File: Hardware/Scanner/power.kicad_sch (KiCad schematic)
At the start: 15 parts, among them J1 I2C ThroughHole, J3 I2C, J4 Interface, U7 AP7312-1833W6-7

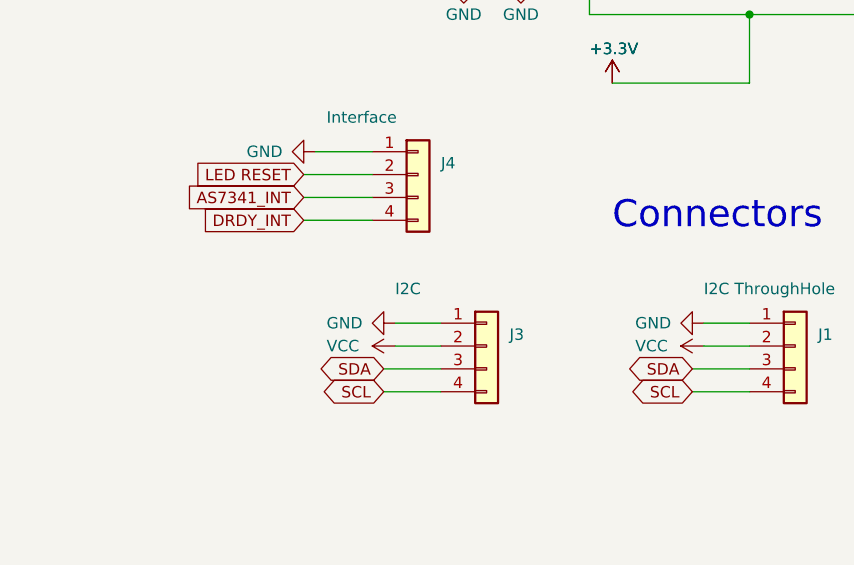
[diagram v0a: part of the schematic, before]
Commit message: added footprint for MTSM2601SMF1-100
Signed-off-by: lokimetasmith <lokimail@gmail.com>
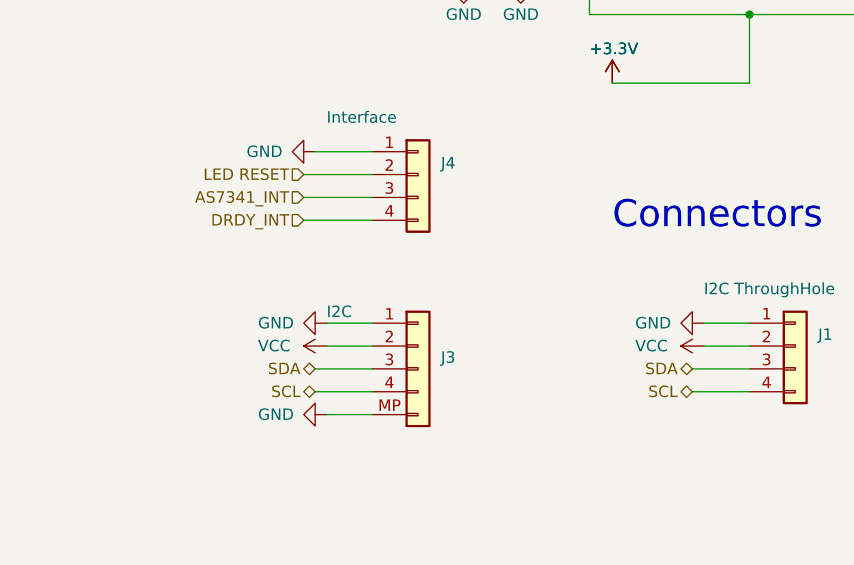
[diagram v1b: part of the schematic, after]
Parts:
- J3: symbol Connector_Generic:Conn_01x04 -> Connector_Generic:Conn_01x05
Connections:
- net GND: now also J3.MP (Pin_5)

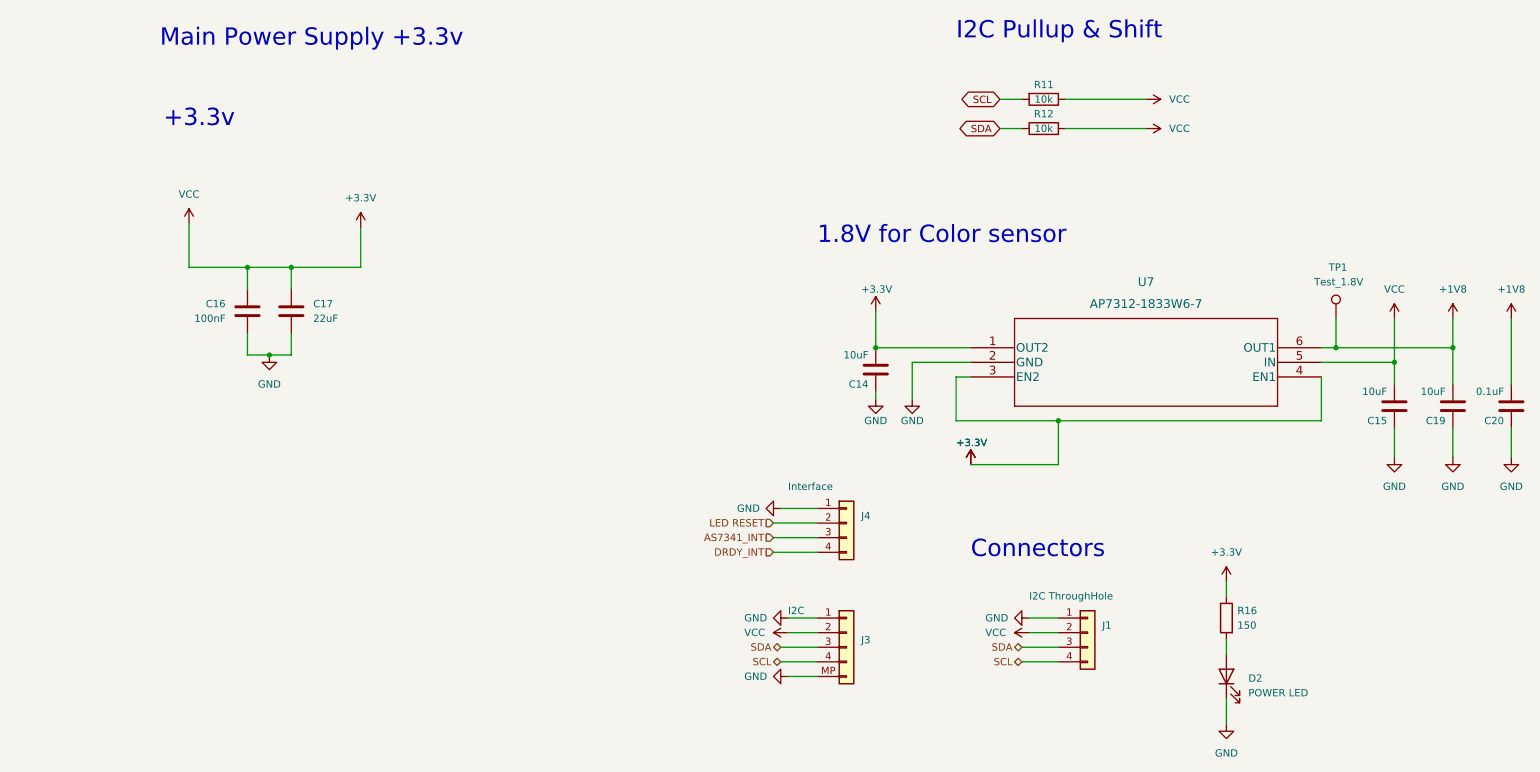
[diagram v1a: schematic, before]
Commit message: lots of changes, added footprints, fixed broken schemaitcs, fixed kicad 7.0 issues
Signed-off-by: lokimetasmith <lokimail@gmail.com>
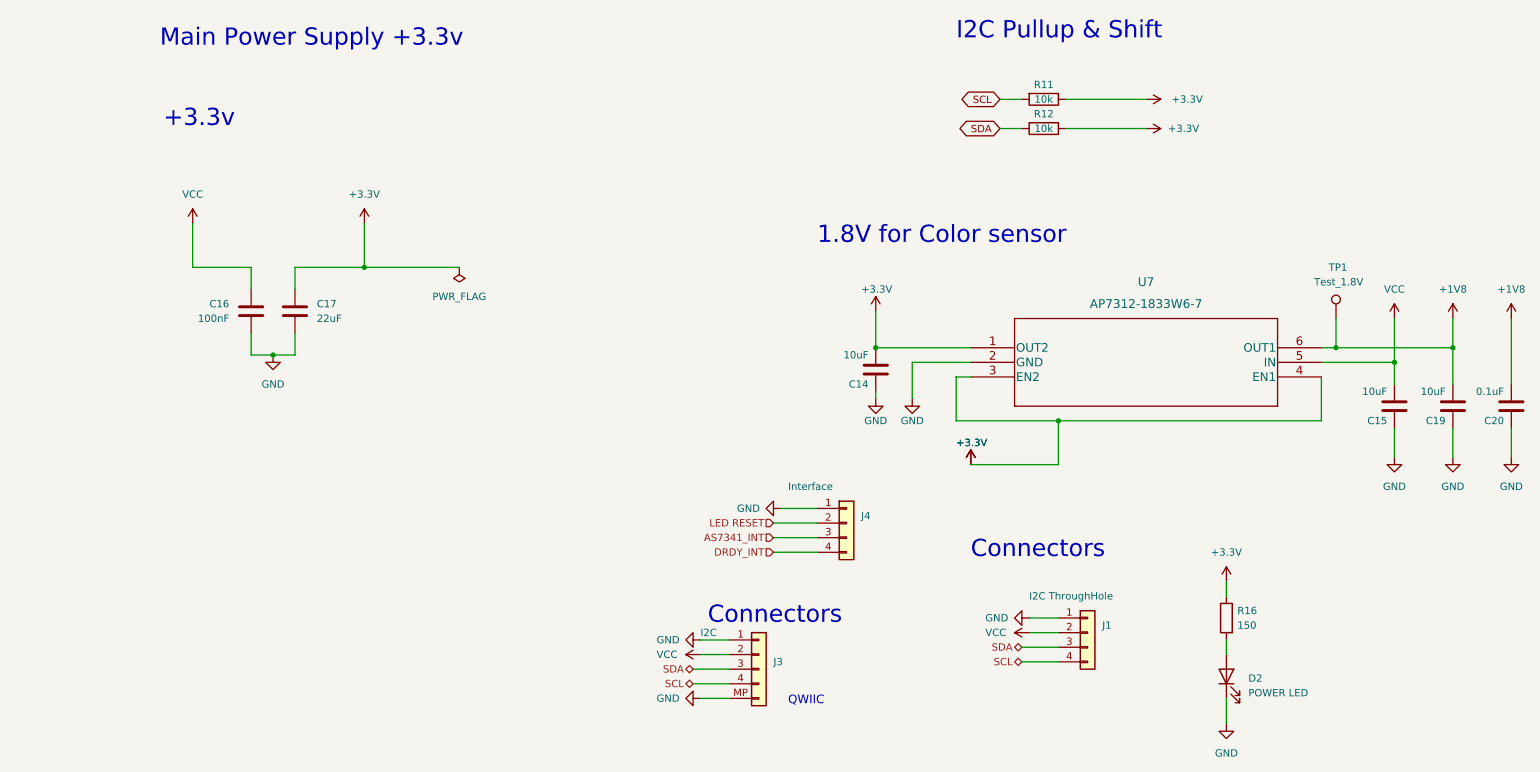
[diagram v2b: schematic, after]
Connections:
- net +3V3 renamed +3.3V
- net +3.3V: no longer C15.2, C16.2, J1.2 (Pin_2), J3.2 (Pin_2), U7.5 (IN)
- new net VCC: C15.2, C16.2, J1.2 (Pin_2), J3.2 (Pin_2), U7.5 (IN)
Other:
- note added: "QWIIC"
- moved on the sheet: C16, C17, J3

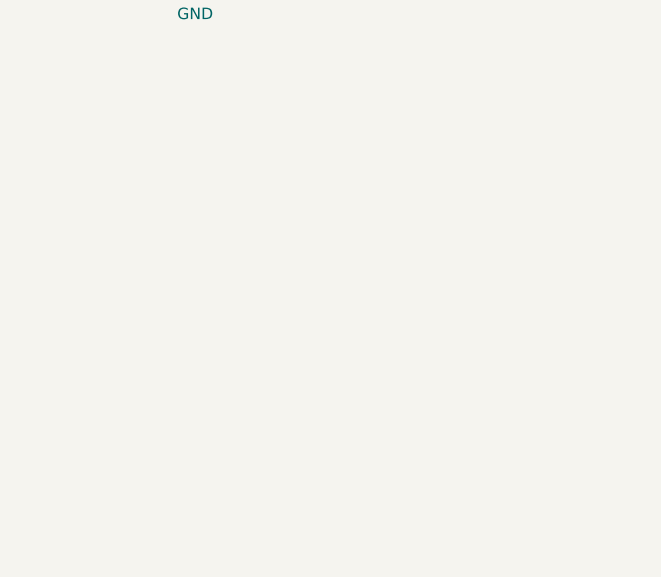
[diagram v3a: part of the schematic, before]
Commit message: added options for using internal adc, external adc, or 3.3v
Signed-off-by: lokimetasmith <lokimail@gmail.com>
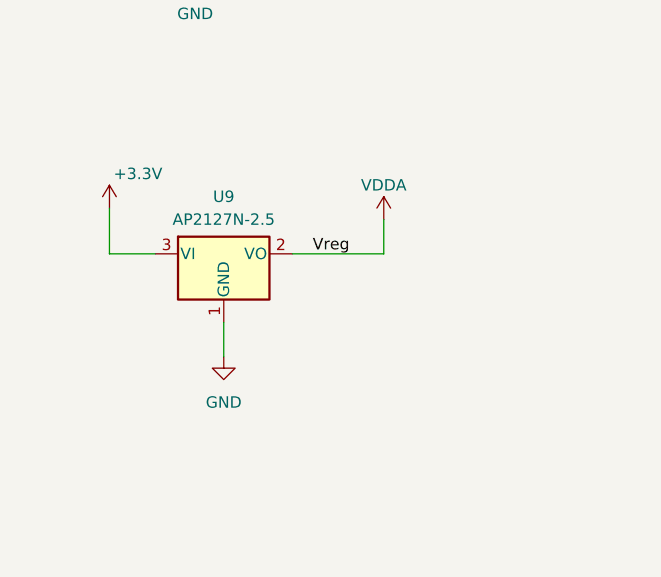
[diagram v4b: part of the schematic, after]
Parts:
- added U9: AP2127N-2.5, Package_TO_SOT_SMD:SOT-23, symbol Regulator_Linear:AP2127N-2.5
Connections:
- net +3.3V: now also U9.3 (VI)
- net GND: now also U9.1 (GND)
- new net VDDA: U9.2 (VO)
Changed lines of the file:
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@@
+    (stroke (width 0) (type default))
+  )
+  (wire (pts (xy 45.72 123.19) (xy 50.8 123.19))
     (stroke (width 0) (type default))
   )
@@
     (stroke (width 0) (type default))
   )
+  (wire (pts (xy 45.72 118.11) (xy 45.72 123.19))
+    (stroke (width 0) (type default))
+  )
   (wire (pts (xy 270.51 104.14) (xy 270.51 109.22))
     (stroke (width 0) (type default))
@@
     (stroke (width 0) (type default))
   )
+  (wire (pts (xy 66.04 123.19) (xy 76.2 123.19))
+    (stroke (width 0) (type default))
+  )
   (wire (pts (xy 173.99 102.87) (xy 173.99 95.25))
     (stroke (width 0) (type default))
@@
   )
   (wire (pts (xy 129.54 143.51) (xy 134.62 143.51))
+    (stroke (width 0) (type default))
+  )
+  (wire (pts (xy 58.42 130.81) (xy 58.42 134.62))
+    (stroke (width 0) (type default))
+  )
+  (wire (pts (xy 76.2 123.19) (xy 76.2 119.38))
     (stroke (width 0) (type default))
   )
@@
   (text "I2C Pullup & Shift\n" (at 173.99 36.83 0)
     (effects (font (size 3 3)) (justify left bottom))
+  )
+  (label "Vreg" (at 72.39 123.19 180) (fields_autoplaced)
+    (effects (font (size 1.27 1.27)) (justify right bottom))
   )
   (global_label "SCL" (shape bidirectional) (at 181.61 46.99 180) (fields_autoplaced)
@@
     )
   )
+  (symbol (lib_id "Regulator_Linear:AP2127N-2.5") (at 58.42 123.19 0) (unit 1)
+    (in_bom yes) (on_board yes) (dnp no) (fields_autoplaced)
+    (property "Reference" "U9" (at 58.42 116.84 0)
+      (effects (font (size 1.27 1.27)))
+    )
+    (property "Value" "AP2127N-2.5" (at 58.42 119.38 0)
+      (effects (font (size 1.27 1.27)))
+    )
+    (property "Footprint" "Package_TO_SOT_SMD:SOT-23" (at 58.42 117.475 0)
+      (effects (font (size 1.27 1.27) italic) hide)
+    )
+    (property "Datasheet" "https://www.diodes.com/assets/Datasheets/AP2127.pdf" (at 58.42 123.19 0)
+      (effects (font (size 1.27 1.27)) hide)
+    )
+    (pin "1")
+    (pin "2")
+    (pin "3")
+    (instances
+      (project "RoundScanner"
+        (path "/a818e058-3544-4da8-96fb-1a428660711f/98df1e87-3735-4cb9-8253-663f6eb2234f"
+          (reference "U9") (unit 1)
+        )
+        (path "/a818e058-3544-4da8-96fb-1a428660711f/5869e7b3-0d61-455b-97ad-e4e8b4829f27"
+          (reference "U9") (unit 1)
+        )
+      )
+    )
+  )
   (symbol (lib_id "power:GND") (at 186.69 137.16 270) (unit 1)
     (in_bom yes) (on_board yes) (dnp no)
@@
         (path "/a818e058-3544-4da8-96fb-1a428660711f/5869e7b3-0d61-455b-97ad-e4e8b4829f27"
           (reference "#PWR033") (unit 1)
+        )
+      )
+    )
+  )
+  (symbol (lib_id "power:VDDA") (at 76.2 119.38 0) (unit 1)
+    (in_bom yes) (on_board yes) (dnp no) (fields_autoplaced)
+    (property "Reference" "#PWR014" (at 76.2 123.19 0)
+      (effects (font (size 1.27 1.27)) hide)
+    )
+    (property "Value" "VDDA" (at 76.2 115.57 0)
+      (effects (font (size 1.27 1.27)))
+    )
+    (property "Footprint" "" (at 76.2 119.38 0)
+      (effects (font (size 1.27 1.27)) hide)
+    )
+    (property "Datasheet" "" (at 76.2 119.38 0)
+      (effects (font (size 1.27 1.27)) hide)
+    )
+    (pin "1")
+    (instances
+      (project "RoundScanner"
+        (path "/a818e058-3544-4da8-96fb-1a428660711f/5869e7b3-0d61-455b-97ad-e4e8b4829f27"
+          (reference "#PWR014") (unit 1)
         )
       )
@@
     )
   )
+  (symbol (lib_id "power:GND") (at 58.42 134.62 0) (unit 1)
+    (in_bom yes) (on_board yes) (dnp no) (fields_autoplaced)
+    (property "Reference" "#PWR011" (at 58.42 140.97 0)
+      (effects (font (size 1.27 1.27)) hide)
+    )
+    (property "Value" "GND" (at 58.42 139.7 0)
+      (effects (font (size 1.27 1.27)))
+    )
+    (property "Footprint" "" (at 58.42 134.62 0)
+      (effects (font (size 1.27 1.27)) hide)
+    )
+    (property "Datasheet" "" (at 58.42 134.62 0)
+      (effects (font (size 1.27 1.27)) hide)
+    )
+    (pin "1")
+    (instances
+      (project "RoundScanner"
+        (path "/a818e058-3544-4da8-96fb-1a428660711f/98df1e87-3735-4cb9-8253-663f6eb2234f"
+          (reference "#PWR011") (unit 1)
+        )
+        (path "/a818e058-3544-4da8-96fb-1a428660711f/5869e7b3-0d61-455b-97ad-e4e8b4829f27"
+          (reference "#PWR013") (unit 1)
+        )
+      )
+    )
+  )
   (symbol (lib_id "power:+1V8") (at 260.35 85.09 0) (unit 1)
     (in_bom yes) (on_board yes) (dnp no) (fields_autoplaced)
@@
         )
       )
+    )
+  )
+  (symbol (lib_id "power:+3.3V") (at 45.72 118.11 0) (unit 1)
+    (in_bom yes) (on_board yes) (dnp no)
+    (property "Reference" "#PWR0136" (at 45.72 121.92 0)
+      (effects (font (size 1.27 1.27)) hide)
+    )
+    (property "Value" "+3.3V" (at 48.895 114.3 0)
+      (effects (font (size 1.27 1.27)))
+    )
+    (property "Footprint" "" (at 45.72 118.11 0)
+      (effects (font (size 1.27 1.27)) hide)
+    )
+    (property "Datasheet" "" (at 45.72 118.11 0)
+      (effects (font (size 1.27 1.27)) hide)
+    )
+    (pin "1")
+    (instances
+      (project "RoundScanner"
+        (path "/a818e058-3544-4da8-96fb-1a428660711f/98df1e87-3735-4cb9-8253-663f6eb2234f"
+          (reference "#PWR0136") (unit 1)
+        )
+        (path "/a818e058-3544-4da8-96fb-1a428660711f/5869e7b3-0d61-455b-97ad-e4e8b4829f27"
+          (reference "#PWR011") (unit 1)
+        )
+      )

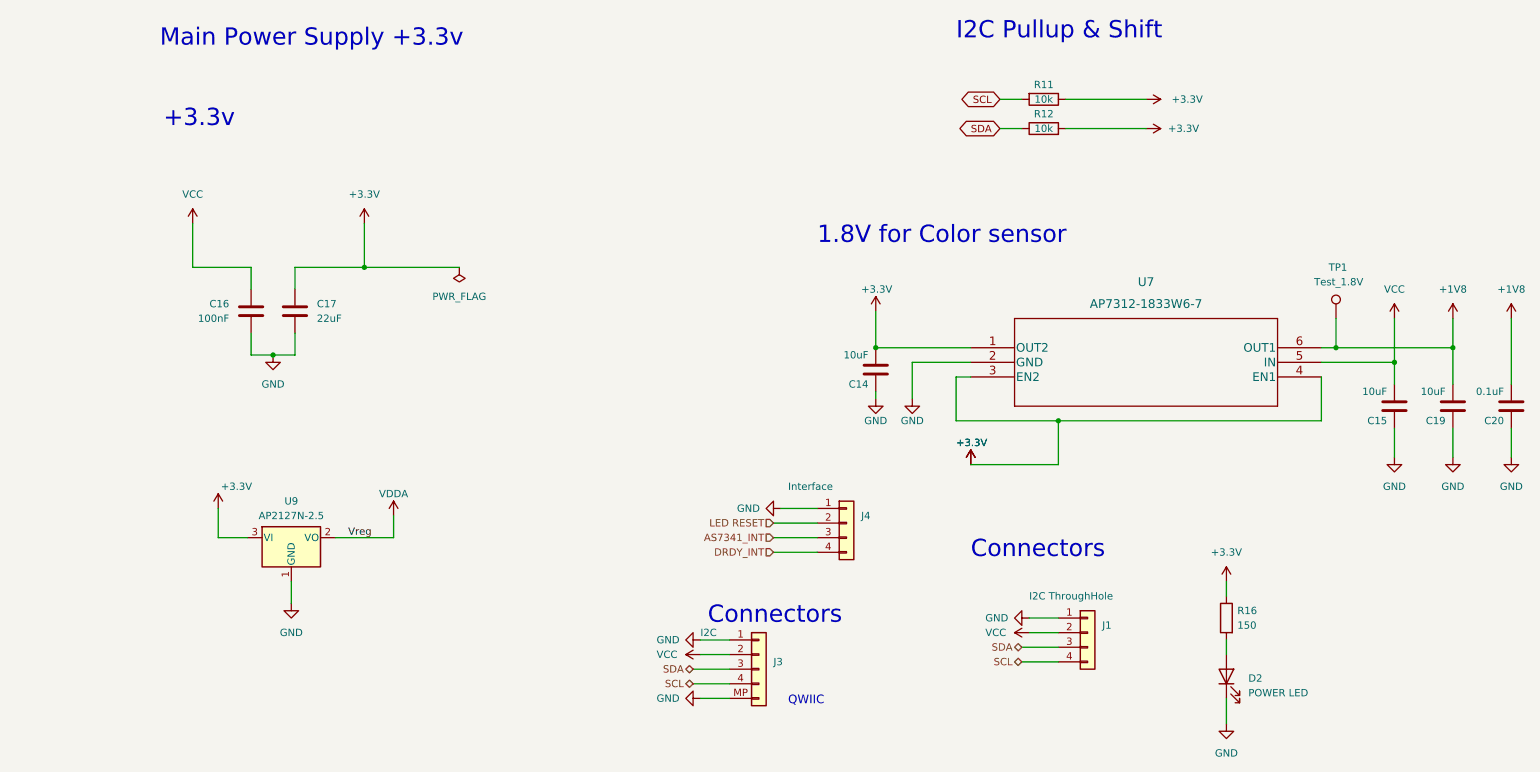
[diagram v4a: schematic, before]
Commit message: updated schematic, and layout, updated bom, fully converted to 3.3v for Voltage input only
Signed-off-by: lokimetasmith <lokimail@gmail.com>
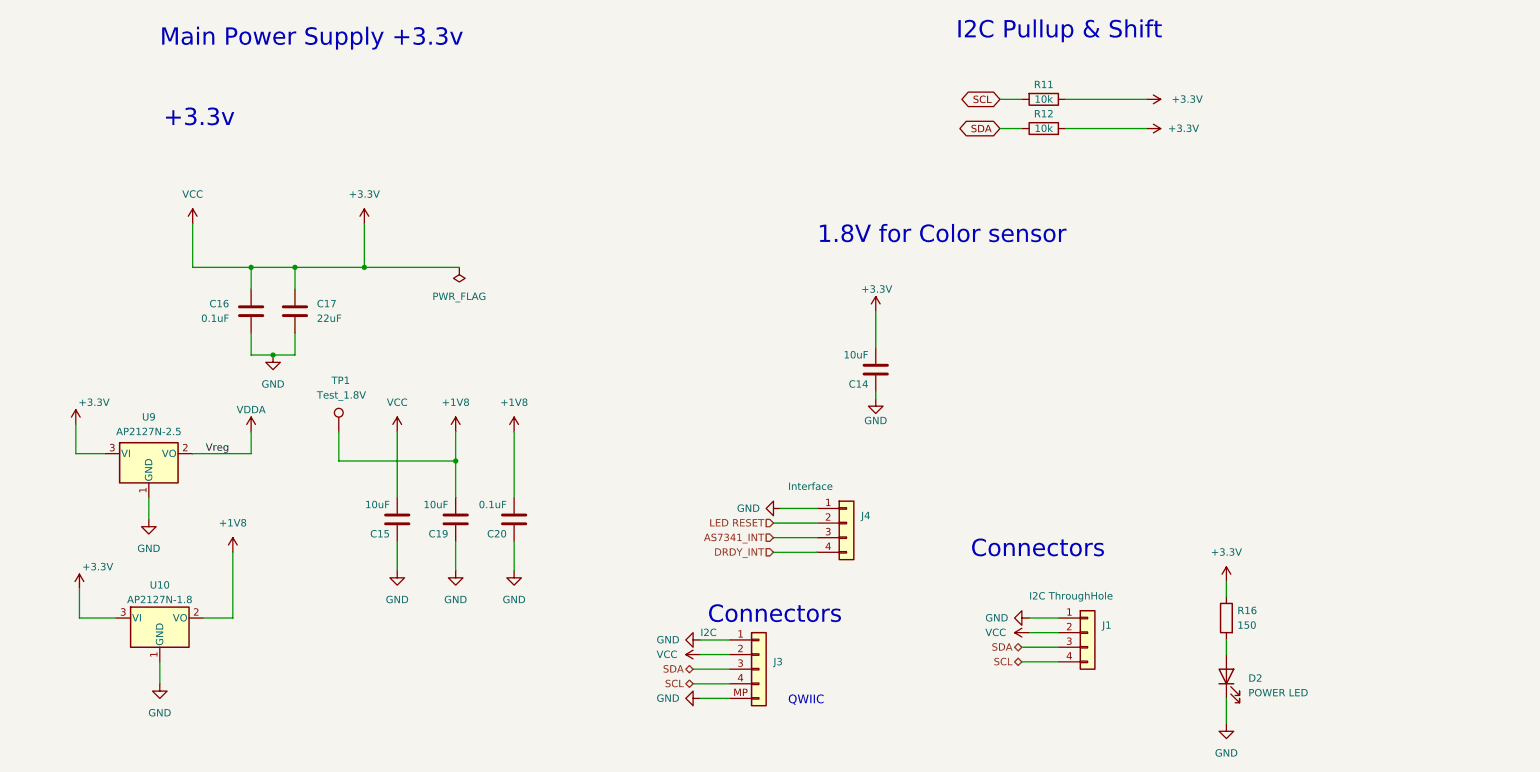
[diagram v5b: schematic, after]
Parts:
- removed U7: AP7312-1833W6-7, AP7312-1833W6-7:AP7312-1833W6-7, symbol AP7312-1833W6-7:AP7312-1833W6-7
- added U10: AP2127N-1.8, Package_TO_SOT_SMD:SOT-23, symbol Regulator_Linear:AP2127N-1.8
- C14, C15, C19: digikey description (none) -> CAP CER 10UF 6.3V X5R 0603; digikey part number (none) -> 1276-1038-1-ND
- C16: value 100nF -> 0.1uF; digikey description (none) -> CAP CER 0.1UF 16V X7R 0603; digikey part number (none) -> 311-1088-1-ND
- C17: digikey description (none) -> CAP CER 22UF 6.3V X5R 0603; digikey part number (none) -> 490-7611-1-ND
- C20: digikey description (none) -> CAP CER 0.1UF 16V X7R 0603; digikey part number (none) -> 311-1088-1-ND
- D2: digikey description (none) -> LED RED CLEAR 1206 SMD; digikey part number (none) -> 160-1405-1-ND
- R11, R12: digikey description (none) -> RES 10K OHM 5% 1/10W 0603; digikey part number (none) -> 311-10KGRCT-ND; mouser description (none) -> CRGH0603J10K; mouser part number (none) -> 279-CRGH0603J10K
- U9: digikey description (none) -> IC REG LINEAR 2.5V 300MA SOT23; digikey part number (none) -> AP2127N-2.5TRG1DI-ND
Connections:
- net VCC is gone; now on net +3.3V: C15.2, C16.2, J1.2 (Pin_2), J3.2 (Pin_2)
- net +1V8: now also U10.2 (VO)
- net +3.3V: now also U10.3 (VI)
- net GND: now also U10.1 (GND)
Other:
- moved on the sheet: C15, C19, C20, TP1, U9
